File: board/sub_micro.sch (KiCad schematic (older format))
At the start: 18 parts, among them J301 ARM SWD, J302 Conn_01x02, J303 Conn_01x09, J304 Conn_01x03, J305 USB_B, U301 STM32F072CBTx, U302 USBLC6-2SC6

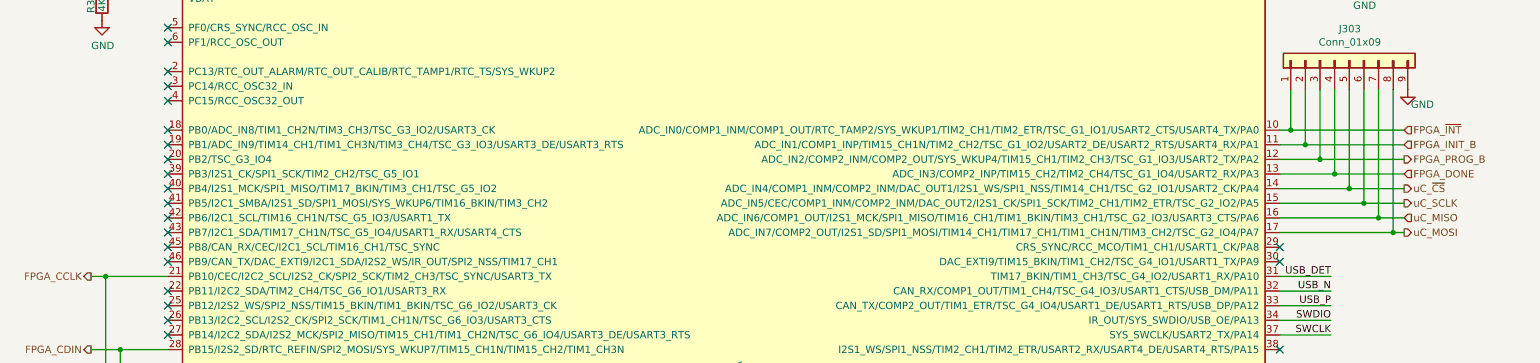
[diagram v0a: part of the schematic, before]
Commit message: Added SPI Flash for uC
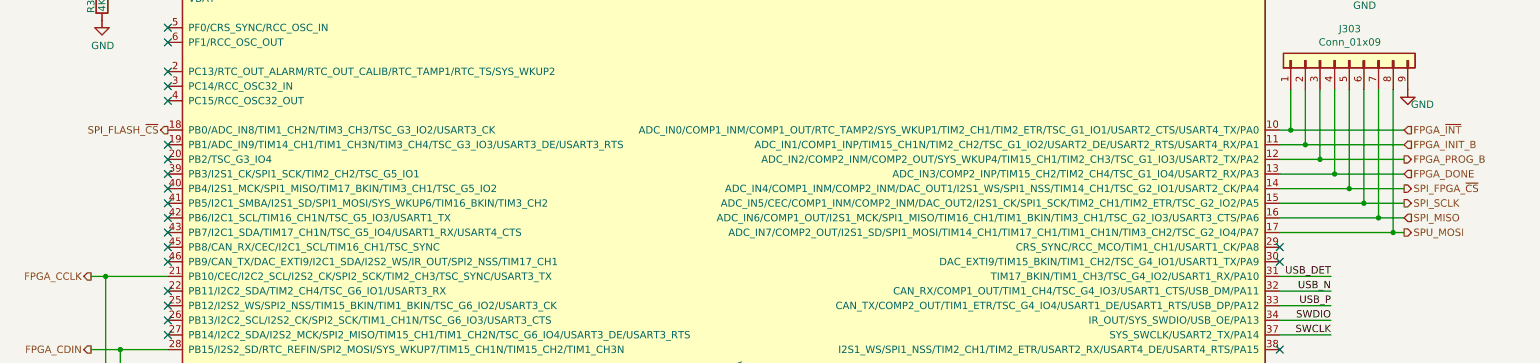
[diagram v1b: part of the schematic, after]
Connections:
- net SPI_FLASH_~CS: now reaches U301.18 (PB0/ADC_IN8/TIM1_CH2N/TIM3_CH3/TSC_G3_IO2/USART3_CK)
- net uC_MISO renamed SPI_MISO
- net uC_MOSI renamed SPU_MOSI
- net uC_SCLK renamed SPI_SCLK
- net uC_~CS renamed SPI_FPGA_~CS
- no-connect marks 25 -> 24
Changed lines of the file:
@@
 $Descr A4 11693 8268
 encoding utf-8
-Sheet 3 14
+Sheet 3 15
 Title ""
 Date ""
@@
 $EndComp
 Text HLabel 9975 4425 2    50   Output ~ 0
-uC_SCLK
+SPI_SCLK
 Text HLabel 9975 4625 2    50   Output ~ 0
-uC_MOSI
+SPU_MOSI
 Text HLabel 9975 4525 2    50   Input ~ 0
-uC_MISO
+SPI_MISO
 Text HLabel 9975 4325 2    50   Output ~ 0
-uC_~CS
+SPI_FPGA_~CS
 Text HLabel 9975 3925 2    50   Input ~ 0
 FPGA_~INT
@@
 NoConn ~ 1525 3625
 NoConn ~ 1525 3725
-NoConn ~ 1525 3925
 NoConn ~ 1525 4025
 NoConn ~ 1525 4125
@@
 Wire Wire Line
 	1000 5600 1000 5650
+Text HLabel 1525 3925 0    50   Output ~ 0
+SPI_FLASH_~CS
 $EndSCHEMATC

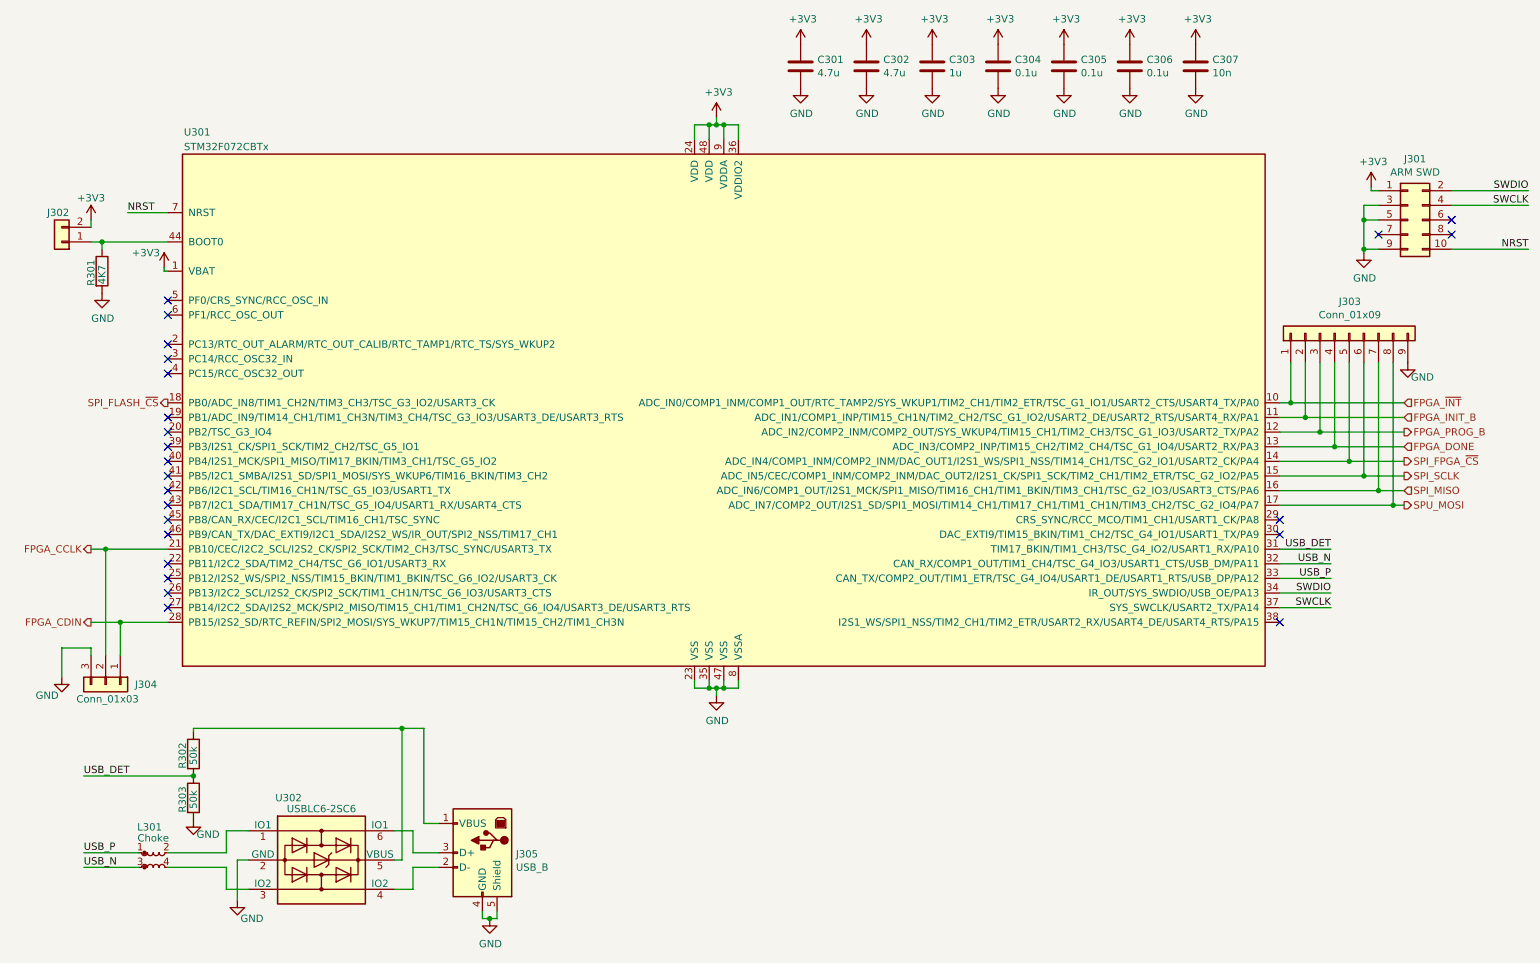
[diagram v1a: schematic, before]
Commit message: Most footprints associated
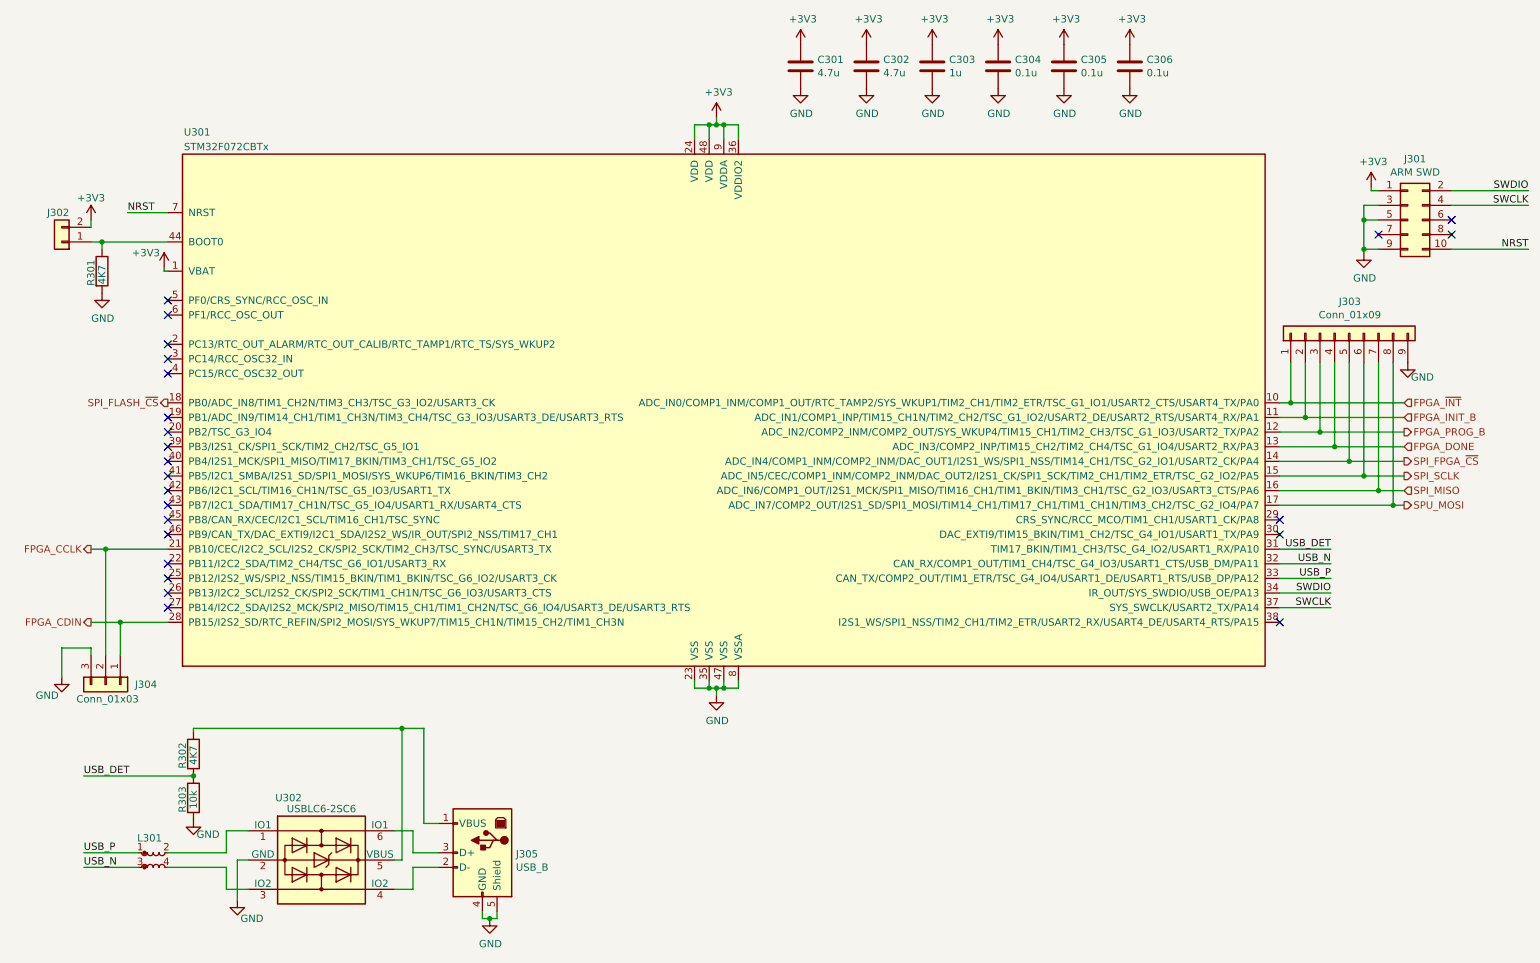
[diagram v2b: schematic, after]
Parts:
- removed C307: 10n, symbol Device:C
- C301, C302, C303, C304, C305, C306: footprint (none) -> Capacitor_SMD:C_0603_1608Metric
- J303: footprint (none) -> Connector_PinHeader_2.54mm:PinHeader_1x09_P2.54mm_Vertical
- J304: footprint (none) -> Connector_PinHeader_2.54mm:PinHeader_1x03_P2.54mm_Vertical
- L301: value Choke -> USB Choke
- R301: footprint (none) -> Resistor_SMD:R_0603_1608Metric
- R302: value 50k -> 4K7; footprint (none) -> Resistor_SMD:R_0603_1608Metric
- R303: value 50k -> 10k; footprint (none) -> Resistor_SMD:R_0603_1608Metric
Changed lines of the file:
@@
 USB_P
 $Comp
-L power:GND #PWR0326
+L power:GND #PWR0324
 U 1 1 5AA58CA8
 P 3725 7450
-F 0 "#PWR0326" H 3725 7200 50  0001 C CNN
+F 0 "#PWR0324" H 3725 7200 50  0001 C CNN
 F 1 "GND" H 3730 7277 50  0000 C CNN
 F 2 "" H 3725 7450 50  0001 C CNN
@@
 Connection ~ 5325 2025
 $Comp
-L power:GND #PWR0323
+L power:GND #PWR0321
 U 1 1 5AA5F8A6
 P 5275 5925
-F 0 "#PWR0323" H 5275 5675 50  0001 C CNN
+F 0 "#PWR0321" H 5275 5675 50  0001 C CNN
 F 1 "GND" H 5280 5752 50  0000 C CNN
 F 2 "" H 5275 5925 50  0001 C CNN
@@
 U 1 1 5AC01C3F
 P 1425 7050
-F 0 "L301" H 1400 7275 50  0000 C CNN
-F 1 "Choke" H 1425 7200 50  0000 C CNN
+F 0 "L301" H 1400 7200 50  0000 C CNN
+F 1 "USB Choke" H 1425 7200 50  0001 C CNN
 F 2 "" H 1425 7050 50  0001 C CNN
 F 3 "~" H 1425 7050 50  0001 C CNN
@@
 P 1700 6625
 F 0 "R303" V 1625 6525 50  0000 L CNN
-F 1 "50k" V 1700 6550 50  0000 L CNN
-F 2 "" V 1630 6625 50  0001 C CNN
+F 1 "10k" V 1700 6550 50  0000 L CNN
+F 2 "Resistor_SMD:R_0603_1608Metric" V 1630 6625 50  0001 C CNN
 F 3 "~" H 1700 6625 50  0001 C CNN
 	1    1700 6625
@@
 P 1700 6325
 F 0 "R302" V 1625 6225 50  0000 L CNN
-F 1 "50k" V 1700 6250 50  0000 L CNN
-F 2 "" V 1630 6325 50  0001 C CNN
+F 1 "4K7" V 1700 6250 50  0000 L CNN
+F 2 "Resistor_SMD:R_0603_1608Metric" V 1630 6325 50  0001 C CNN
 F 3 "~" H 1700 6325 50  0001 C CNN
 	1    1700 6325
@@
 	1700 6150 1700 6175
 $Comp
-L power:GND #PWR0324
+L power:GND #PWR0322
 U 1 1 5AC0839F
 P 1700 6775
-F 0 "#PWR0324" H 1700 6525 50  0001 C CNN
+F 0 "#PWR0322" H 1700 6525 50  0001 C CNN
 F 1 "GND" H 1800 6675 50  0000 C CNN
 F 2 "" H 1700 6775 50  0001 C CNN
@@
 	2000 7050 2000 7325
 $Comp
-L power:GND #PWR0325
+L power:GND #PWR0323
 U 1 1 5AAE95B9
 P 2000 7325
-F 0 "#PWR0325" H 2000 7075 50  0001 C CNN
+F 0 "#PWR0323" H 2000 7075 50  0001 C CNN
 F 1 "GND" H 2100 7200 50  0000 C CNN
 F 2 "" H 2000 7325 50  0001 C CNN
@@
 $EndComp
 $Comp
-L power:+3V3 #PWR0315
+L power:+3V3 #PWR0313
 U 1 1 5ACEDF55
 P 5275 1975
-F 0 "#PWR0315" H 5275 1825 50  0001 C CNN
+F 0 "#PWR0313" H 5275 1825 50  0001 C CNN
 F 1 "+3V3" H 5290 2148 50  0000 C CNN
 F 2 "" H 5275 1975 50  0001 C CNN
@@
 $EndComp
 $Comp
-L power:+3V3 #PWR0319
+L power:+3V3 #PWR0317
 U 1 1 5AF89207
 P 1500 3000
-F 0 "#PWR0319" H 1500 2850 50  0001 C CNN
+F 0 "#PWR0317" H 1500 2850 50  0001 C CNN
 F 1 "+3V3" H 1375 3100 50  0000 C CNN
 F 2 "" H 1500 3000 50  0001 C CNN
@@
 	1500 3025 1525 3025
 $Comp
-L power:GND #PWR0313
+L power:GND #PWR0312
 U 1 1 5AF8A29C
 P 8100 1775
-F 0 "#PWR0313" H 8100 1525 50  0001 C CNN
+F 0 "#PWR0312" H 8100 1525 50  0001 C CNN
 F 1 "GND" H 8105 1602 50  0000 C CNN
 F 2 "" H 8100 1775 50  0001 C CNN
@@
 F 0 "C305" H 7765 1671 50  0000 L CNN
 F 1 "0.1u" H 7765 1580 50  0000 L CNN
-F 2 "" H 7688 1475 50  0001 C CNN
+F 2 "Capacitor_SMD:C_0603_1608Metric" H 7688 1475 50  0001 C CNN
 F 3 "~" H 7650 1625 50  0001 C CNN
 	1    7650 1625
@@
 $EndComp
 $Comp
-L power:GND #PWR0312
+L power:GND #PWR0311
 U 1 1 5AF8A378
 P 7650 1775
-F 0 "#PWR0312" H 7650 1525 50  0001 C CNN
+F 0 "#PWR0311" H 7650 1525 50  0001 C CNN
 F 1 "GND" H 7655 1602 50  0000 C CNN
 F 2 "" H 7650 1775 50  0001 C CNN
@@
 F 0 "C304" H 7315 1671 50  0000 L CNN
 F 1 "0.1u" H 7315 1580 50  0000 L CNN
-F 2 "" H 7238 1475 50  0001 C CNN
+F 2 "Capacitor_SMD:C_0603_1608Metric" H 7238 1475 50  0001 C CNN
 F 3 "~" H 7200 1625 50  0001 C CNN
 	1    7200 1625
@@
 $EndComp
 $Comp
-L power:GND #PWR0311
+L power:GND #PWR0310
 U 1 1 5AF8B1E6
 P 7200 1775
-F 0 "#PWR0311" H 7200 1525 50  0001 C CNN
+F 0 "#PWR0310" H 7200 1525 50  0001 C CNN
 F 1 "GND" H 7205 1602 50  0000 C CNN
 F 2 "" H 7200 1775 50  0001 C CNN
@@
 F 0 "C302" H 6415 1671 50  0000 L CNN
 F 1 "4.7u" H 6415 1580 50  0000 L CNN
-F 2 "" H 6338 1475 50  0001 C CNN
+F 2 "Capacitor_SMD:C_0603_1608Metric" H 6338 1475 50  0001 C CNN
 F 3 "~" H 6300 1625 50  0001 C CNN
 	1    6300 1625
@@
 $EndComp
 $Comp
-L power:GND #PWR0309
+L power:GND #PWR0308
 U 1 1 5AF8B1F8
 P 6300 1775
-F 0 "#PWR0309" H 6300 1525 50  0001 C CNN
+F 0 "#PWR0308" H 6300 1525 50  0001 C CNN
 F 1 "GND" H 6305 1602 50  0000 C CNN
 F 2 "" H 6300 1775 50  0001 C CNN
@@
 F 0 "C303" H 6865 1671 50  0000 L CNN
 F 1 "1u" H 6865 1580 50  0000 L CNN
-F 2 "" H 6788 1475 50  0001 C CNN
+F 2 "Capacitor_SMD:C_0603_1608Metric" H 6788 1475 50  0001 C CNN
 F 3 "~" H 6750 1625 50  0001 C CNN
 	1    6750 1625
@@
 $EndComp
 $Comp
-L power:GND #PWR0310
+L power:GND #PWR0309
 U 1 1 5AF909D9
 P 6750 1775
-F 0 "#PWR0310" H 6750 1525 50  0001 C CNN
+F 0 "#PWR0309" H 6750 1525 50  0001 C CNN
 F 1 "GND" H 6755 1602 50  0000 C CNN
 F 2 "" H 6750 1775 50  0001 C CNN
 F 3 "" H 6750 1775 50  0001 C CNN
 	1    6750 1775
-	1    0    0    -1
-$EndComp
-$Comp
-L Device:C C307
-U 1 1 5AF91996
-P 8550 1625
-F 0 "C307" H 8665 1671 50  0000 L CNN
-F 1 "10n" H 8665 1580 50  0000 L CNN
-F 2 "" H 8588 1475 50  0001 C CNN
-F 3 "~" H 8550 1625 50  0001 C CNN
-	1    8550 1625
-	1    0    0    -1
-$EndComp
-$Comp
-L power:+3V3 #PWR0307
-U 1 1 5AF9199C
-P 8550 1475
-F 0 "#PWR0307" H 8550 1325 50  0001 C CNN
-F 1 "+3V3" H 8565 1648 50  0000 C CNN
-F 2 "" H 8550 1475 50  0001 C CNN
-F 3 "" H 8550 1475 50  0001 C CNN
-	1    8550 1475
-	1    0    0    -1
-$EndComp
-$Comp
-L power:GND #PWR0314
-U 1 1 5AF919A2
-P 8550 1775
-F 0 "#PWR0314" H 8550 1525 50  0001 C CNN
-F 1 "GND" H 8555 1602 50  0000 C CNN
-F 2 "" H 8550 1775 50  0001 C CNN
-F 3 "" H 8550 1775 50  0001 C CNN
-	1    8550 1775
 	1    0    0    -1
 $EndComp
@@
 F 0 "C306" H 8215 1671 50  0000 L CNN
 F 1 "0.1u" H 8215 1580 50  0000 L CNN
-F 2 "" H 8138 1475 50  0001 C CNN
+F 2 "Capacitor_SMD:C_0603_1608Metric" H 8138 1475 50  0001 C CNN
 F 3 "~" H 8100 1625 50  0001 C CNN
 	1    8100 1625
@@
 F 0 "C301" H 5965 1671 50  0000 L CNN
 F 1 "4.7u" H 5965 1580 50  0000 L CNN
-F 2 "" H 5888 1475 50  0001 C CNN
+F 2 "Capacitor_SMD:C_0603_1608Metric" H 5888 1475 50  0001 C CNN
 F 3 "~" H 5850 1625 50  0001 C CNN
 	1    5850 1625
@@
 $EndComp
 $Comp
-L power:GND #PWR0308
+L power:GND #PWR0307
 U 1 1 5AF9435B
 P 5850 1775
-F 0 "#PWR0308" H 5850 1525 50  0001 C CNN
+F 0 "#PWR0307" H 5850 1525 50  0001 C CNN
 F 1 "GND" H 5855 1602 50  0000 C CNN
 F 2 "" H 5850 1775 50  0001 C CNN
@@
 $EndComp
 $Comp
-L power:+3V3 #PWR0317
+L power:+3V3 #PWR0315
 U 1 1 5AF9BD8E
 P 1000 2675
-F 0 "#PWR0317" H 1000 2525 50  0001 C CNN
+F 0 "#PWR0315" H 1000 2525 50  0001 C CNN
 F 1 "+3V3" H 1000 2825 50  0000 C CNN
 F 2 "" H 1000 2675 50  0001 C CNN
@@
 F 0 "R301" V 1000 2925 50  0000 L CNN
 F 1 "4K7" V 1075 2935 50  0000 L CNN
-F 2 "" V 1005 3025 50  0001 C CNN
+F 2 "Resistor_SMD:R_0603_1608Metric" V 1005 3025 50  0001 C CNN
 F 3 "~" H 1075 3025 50  0001 C CNN
 	1    1075 3025
@@
 $EndComp
 $Comp
-L power:GND #PWR0320
+L power:GND #PWR0318
 U 1 1 5AF9E7D2
 P 1075 3175
-F 0 "#PWR0320" H 1075 2925 50  0001 C CNN
+F 0 "#PWR0318" H 1075 2925 50  0001 C CNN
 F 1 "GND" H 1080 3002 50  0000 C CNN
 F 2 "" H 1075 3175 50  0001 C CNN
@@
 NoConn ~ 9800 2775
 $Comp
-L power:+3V3 #PWR0316
+L power:+3V3 #PWR0314
 U 1 1 5AFB780D
 P 9750 2450
-F 0 "#PWR0316" H 9750 2300 50  0001 C CNN
+F 0 "#PWR0314" H 9750 2300 50  0001 C CNN
 F 1 "+3V3" H 9765 2623 50  0000 C CNN
 F 2 "" H 9750 2450 50  0001 C CNN
@@
 	9750 2475 9800 2475
 $Comp
-L power:GND #PWR0318
+L power:GND #PWR0316
 U 1 1 5AFB8DC9
 P 9700 2900
-F 0 "#PWR0318" H 9700 2650 50  0001 C CNN
+F 0 "#PWR0316" H 9700 2650 50  0001 C CNN
 F 1 "GND" H 9705 2727 50  0000 C CNN
 F 2 "" H 9700 2900 50  0001 C CNN
@@
 F 0 "J303" V 9817 3446 50  0000 C CNN
 F 1 "Conn_01x09" V 9726 3446 50  0000 C CNN
-F 2 "" H 9600 3450 50  0001 C CNN
+F 2 "Connector_PinHeader_2.54mm:PinHeader_1x09_P2.54mm_Vertical" H 9600 3450 50  0001 C CNN
 F 3 "~" H 9600 3450 50  0001 C CNN
 	1    9600 3450
@@
 $EndComp
 $Comp
-L power:GND #PWR0321
+L power:GND #PWR0319
 U 1 1 5AB29B43
 P 10000 3650
-F 0 "#PWR0321" H 10000 3400 50  0001 C CNN
+F 0 "#PWR0319" H 10000 3400 50  0001 C CNN
 F 1 "GND" H 10100 3550 50  0000 C CNN
 F 2 "" H 10000 3650 50  0001 C CNN
@@
 F 0 "J304" V 1100 6050 50  0000 L CNN
 F 1 "Conn_01x03" V 1200 5650 50  0000 L CNN
-F 2 "" H 1100 5850 50  0001 C CNN
+F 2 "Connector_PinHeader_2.54mm:PinHeader_1x03_P2.54mm_Vertical" H 1100 5850 50  0001 C CNN
 F 3 "~" H 1100 5850 50  0001 C CNN
 	1    1100 5850
@@
 	1200 5425 1525 5425
 $Comp
-L power:GND #PWR0322
+L power:GND #PWR0320
 U 1 1 5AB4029B
 P 800 5800
-F 0 "#PWR0322" H 800 5550 50  0001 C CNN
+F 0 "#PWR0320" H 800 5550 50  0001 C CNN
 F 1 "GND" H 700 5675 50  0000 C CNN
 F 2 "" H 800 5800 50  0001 C CNN

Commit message: All footprints done
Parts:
- J305: footprint (none) -> quokka:UE27BCX4
- L301: footprint (none) -> quokka:DLW21H
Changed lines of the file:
@@
 F 0 "J305" H 3446 6991 50  0000 R CNN
 F 1 "USB_B" H 3446 6900 50  0000 R CNN
-F 2 "" H 3825 6950 50  0001 C CNN
+F 2 "quokka:UE27BCX4" H 3825 6950 50  0001 C CNN
 F 3 "" H 3825 6950 50  0001 C CNN
 	1    3675 7000
@@
 F 0 "L301" H 1400 7200 50  0000 C CNN
 F 1 "USB Choke" H 1425 7200 50  0001 C CNN
-F 2 "" H 1425 7050 50  0001 C CNN
+F 2 "quokka:DLW21H" H 1425 7050 50  0001 C CNN
 F 3 "~" H 1425 7050 50  0001 C CNN
 	1    1425 7050

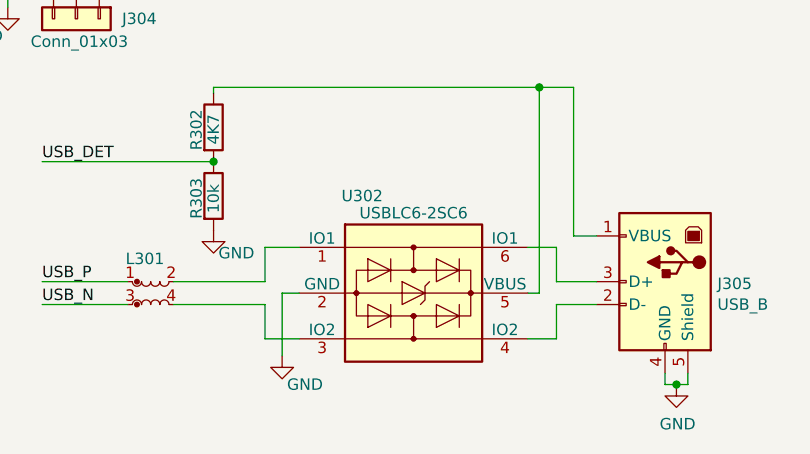
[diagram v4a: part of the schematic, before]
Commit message: Power supply routed
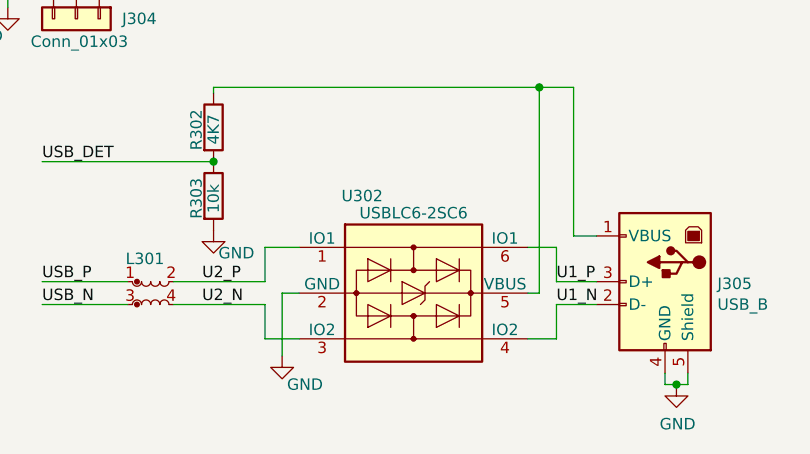
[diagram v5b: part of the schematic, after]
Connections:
- net U1_N: now reaches J305.2 (D-), U302.4 (IO2)
- net U1_P: now reaches J305.3 (D+), U302.6 (IO1)
- net U2_P: now reaches L301.2, U302.1 (IO1)
- net U2_N: now reaches L301.4, U302.3 (IO2)
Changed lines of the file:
@@
 Wire Wire Line
 	950  7000 1325 7000
+Text Label 3200 7100 0    50   ~ 0
+U1_N
+Text Label 3200 7000 0    50   ~ 0
+U1_P
+Text Label 1650 7000 0    50   ~ 0
+U2_P
+Text Label 1650 7100 0    50   ~ 0
+U2_N
 $EndSCHEMATC
